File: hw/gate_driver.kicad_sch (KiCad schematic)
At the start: 0 parts

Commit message: parts of gate driver
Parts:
- added C501, C502: 10uF, Capacitor_SMD:C_0402_1005Metric, symbol Device:C_Small
- added R501, R502: 20k, Resistor_SMD:R_0402_1005Metric, symbol Device:R_Small
- added U501: LMG1210RVRT, IC_LMG1210RVRT, symbol LMG1210RVRT:LMG1210RVRT
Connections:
- new net: R502.1, U501.5 (DHL)
- new net: U501.13 (HS), U501.16 (HS), U501.21 (HS), U501.21_1 (HS), U501.21_2 (HS), U501.9 (HS)
- new net: R501.1, U501.6 (DLH)
- new net +12V: C502.1, U501.2 (VIN)
- new net +5V: C501.1, U501.4 (VDD)
- new net GND: C501.2, C502.2, R501.2, R502.2, U501.20 (VSS), U501.20_1 (VSS), U501.20_2 (VSS), U501.3 (VSS), U501.7 (VSS)
- new net PWM: U501.19 (PWM/LI)
- new net PWM_EN: U501.18 (EN/HI)
- new net SW1_OUT: U501.8 (LO)
- new net SW2_OUT: U501.10 (HO)
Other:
- note added: "Reselect after redeterming deadtime."

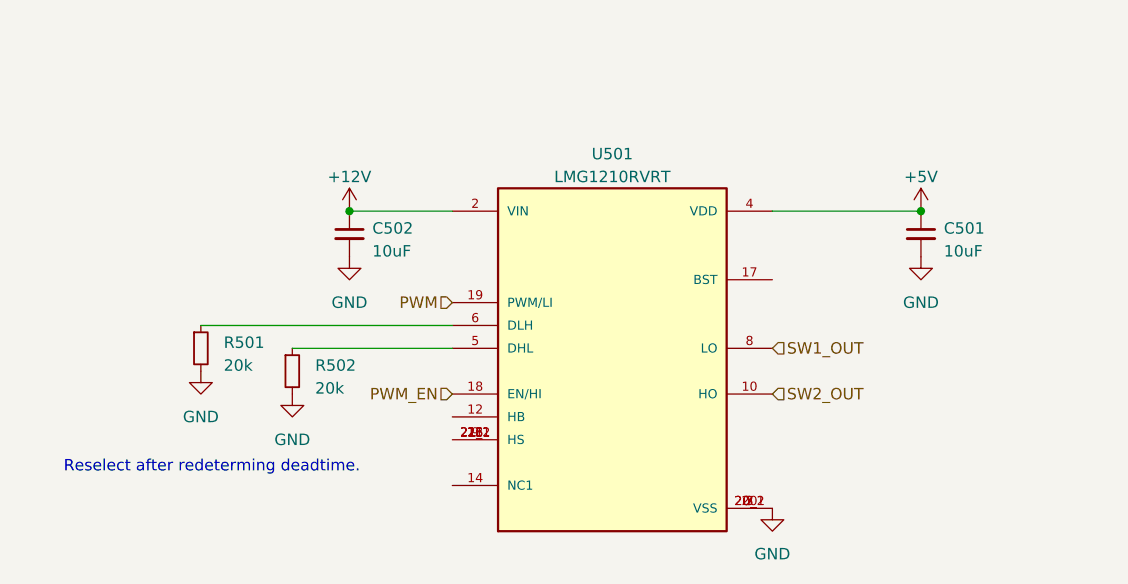
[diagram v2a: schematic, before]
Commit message: laid out MOSFET switching loop and thermal connections
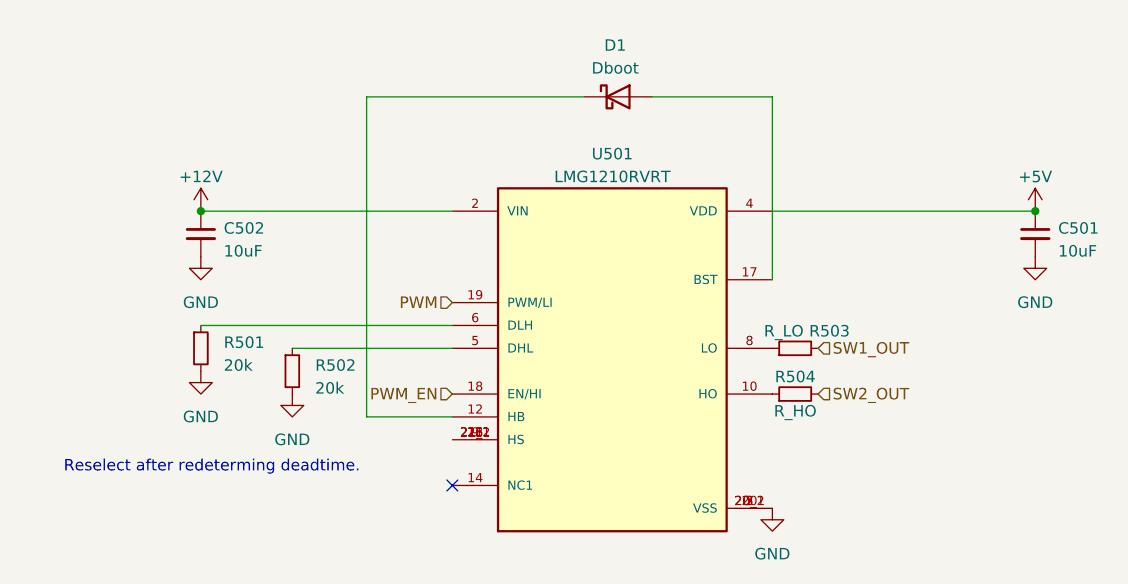
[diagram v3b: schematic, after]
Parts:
- added D1: Dboot, symbol Device:D_Schottky
- added R503: R_LO, Resistor_SMD:R_0402_1005Metric, symbol Device:R_Small
- added R504: R_HO, Resistor_SMD:R_0402_1005Metric, symbol Device:R_Small
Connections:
- net SW1_OUT: now also R503.2; no longer U501.8 (LO)
- net SW2_OUT: now also R504.2; no longer U501.10 (HO)
- net at U501.12 (HB): now also D1.1 (K)
- net at U501.17 (BST): now also D1.2 (A)
- new net: R504.1, U501.10 (HO)
- new net: R503.1, U501.8 (LO)
- no-connect marks 0 -> 1
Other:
- moved on the sheet: C501, C502

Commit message: made gate driver loop v1
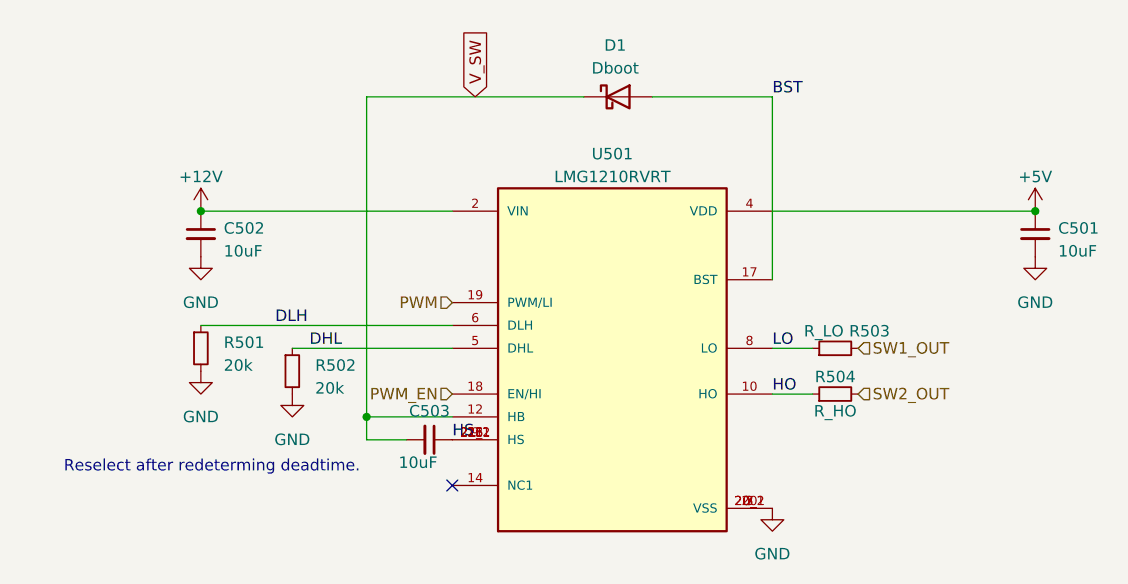
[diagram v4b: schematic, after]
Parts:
- added C503: 10uF, Capacitor_SMD:C_0402_1005Metric, symbol Device:C_Small
- C501: Mfg PN (none) -> GRM158R61A226ME15D
- C502: footprint Capacitor_SMD:C_0402_1005Metric -> Capacitor_SMD:C_0603_1608Metric; Mfg PN (none) -> CL10A226MO7JZNC
- D1: footprint (none) -> Diode_SMD:D_SOD-323
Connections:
- net HO: now reaches R504.1, U501.10 (HO)
- net LO: now reaches R503.1, U501.8 (LO)
- net V_SW: now reaches D1.1 (K), U501.12 (HB)
- net V_SW: now also C503.2
- net BST: now reaches D1.2 (A), U501.17 (BST)
- net DHL: now reaches R502.1, U501.5 (DHL)
- net HS: now reaches U501.13 (HS), U501.16 (HS), U501.21 (HS), U501.21_1 (HS), U501.21_2 (HS), U501.9 (HS)
- net HS: now also C503.1
- net DLH: now reaches R501.1, U501.6 (DLH)
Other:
- moved on the sheet: R503, R504
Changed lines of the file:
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@@
     (comment 2 "Jacob Pustilnik")
   )
+  (junction (at 128.905 101.6) (diameter 0) (color 0 0 0 0)
+  )
   (junction (at 203.2 78.74) (diameter 0) (color 0 0 0 0)
   )
@@
   )
   (no_connect (at 138.43 109.22))
-  (wire (pts (xy 128.905 101.6) (xy 128.905 66.04))
+  (wire (pts (xy 173.99 99.06) (xy 178.435 99.06))
+    (stroke (width 0) (type default))
+  )
+  (wire (pts (xy 128.905 66.04) (xy 128.905 101.6))
+    (stroke (width 0) (type default))
+  )
+  (wire (pts (xy 128.905 101.6) (xy 138.43 101.6))
     (stroke (width 0) (type default))
   )
@@
     (stroke (width 0) (type default))
   )
-  (wire (pts (xy 138.43 101.6) (xy 128.905 101.6))
-    (stroke (width 0) (type default))
-  )
   (wire (pts (xy 160.655 66.04) (xy 173.99 66.04))
     (stroke (width 0) (type default))
   )
+  (wire (pts (xy 173.99 93.98) (xy 178.435 93.98))
+    (stroke (width 0) (type default))
+  )
+  (wire (pts (xy 133.35 104.14) (xy 128.905 104.14))
+    (stroke (width 0) (type default))
+  )
   (wire (pts (xy 173.99 66.04) (xy 173.99 86.36))
     (stroke (width 0) (type default))
@@
     (stroke (width 0) (type default))
   )
+  (wire (pts (xy 128.905 101.6) (xy 128.905 104.14))
+    (stroke (width 0) (type default))
+  )
   (wire (pts (xy 110.49 91.44) (xy 138.43 91.44))
     (stroke (width 0) (type default))
@@
     (effects (font (size 1.27 1.27)) (justify left bottom))
   )
-  (hierarchical_label "SW2_OUT" (shape input) (at 179.07 99.06 0) (fields_autoplaced)
+  (label "DHL" (at 122.555 93.98 0) (fields_autoplaced)
+    (effects (font (size 1.27 1.27)) (justify left bottom))
+  )
+  (label "HO" (at 173.99 99.06 0) (fields_autoplaced)
+    (effects (font (size 1.27 1.27)) (justify left bottom))
+  )
+  (label "HS" (at 138.43 104.14 0) (fields_autoplaced)
+    (effects (font (size 1.27 1.27)) (justify left bottom))
+  )
+  (label "BST" (at 173.99 66.04 0) (fields_autoplaced)
+    (effects (font (size 1.27 1.27)) (justify left bottom))
+  )
+  (label "DLH" (at 118.745 91.44 0) (fields_autoplaced)
+    (effects (font (size 1.27 1.27)) (justify left bottom))
+  )
+  (label "LO" (at 173.99 93.98 0) (fields_autoplaced)
+    (effects (font (size 1.27 1.27)) (justify left bottom))
+  )
+  (global_label "V_SW" (shape input) (at 140.97 66.04 90) (fields_autoplaced)
+    (effects (font (size 1.27 1.27)) (justify left))
+    (property "Intersheetrefs" "${INTERSHEET_REFS}" (at 140.97 58.4171 90)
+      (effects (font (size 1.27 1.27)) (justify left) hide)
+    )
+  )
+  (hierarchical_label "SW2_OUT" (shape input) (at 183.515 99.06 0) (fields_autoplaced)
     (effects (font (size 1.27 1.27)) (justify left))
   )
@@
     (effects (font (size 1.27 1.27)) (justify right))
   )
-  (hierarchical_label "SW1_OUT" (shape input) (at 179.07 93.98 0) (fields_autoplaced)
+  (hierarchical_label "SW1_OUT" (shape input) (at 183.515 93.98 0) (fields_autoplaced)
     (effects (font (size 1.27 1.27)) (justify left))
   )
-  (symbol (lib_id "Device:R_Small") (at 176.53 99.06 90) (unit 1)
+  (symbol (lib_id "Device:R_Small") (at 180.975 99.06 90) (unit 1)
     (in_bom yes) (on_board yes) (dnp no)
-    (property "Reference" "R504" (at 176.53 97.155 90)
-      (effects (font (size 1.27 1.27)))
-    )
-    (property "Value" "R_HO" (at 176.53 100.965 90)
-      (effects (font (size 1.27 1.27)))
-    )
-    (property "Footprint" "Resistor_SMD:R_0402_1005Metric" (at 176.53 99.06 0)
-      (effects (font (size 1.27 1.27)) hide)
-    )
-    (property "Datasheet" "~" (at 176.53 99.06 0)
+    (property "Reference" "R504" (at 180.975 97.155 90)
+      (effects (font (size 1.27 1.27)))
+    )
+    (property "Value" "R_HO" (at 180.975 100.965 90)
+      (effects (font (size 1.27 1.27)))
+    )
+    (property "Footprint" "Resistor_SMD:R_0402_1005Metric" (at 180.975 99.06 0)
+      (effects (font (size 1.27 1.27)) hide)
+    )
+    (property "Datasheet" "~" (at 180.975 99.06 0)
       (effects (font (size 1.27 1.27)) hide)
     )
@@
       (effects (font (size 1.27 1.27)) hide)
     )
+    (property "Mfg PN" "GRM158R61A226ME15D" (at 203.2 81.28 0)
+      (effects (font (size 1.27 1.27)) hide)
+    )
     (pin "1")
     (pin "2")
@@
     )
   )
-  (symbol (lib_id "Device:R_Small") (at 176.53 93.98 90) (unit 1)
+  (symbol (lib_id "Device:R_Small") (at 180.975 93.98 90) (unit 1)
     (in_bom yes) (on_board yes) (dnp no)
-    (property "Reference" "R503" (at 180.34 92.075 90)
-      (effects (font (size 1.27 1.27)))
-    )
-    (property "Value" "R_LO" (at 175.26 92.075 90)
-      (effects (font (size 1.27 1.27)))
-    )
-    (property "Footprint" "Resistor_SMD:R_0402_1005Metric" (at 176.53 93.98 0)
-      (effects (font (size 1.27 1.27)) hide)
-    )
-    (property "Datasheet" "~" (at 176.53 93.98 0)
+    (property "Reference" "R503" (at 184.785 92.075 90)
+      (effects (font (size 1.27 1.27)))
+    )
+    (property "Value" "R_LO" (at 179.705 92.075 90)
+      (effects (font (size 1.27 1.27)))
+    )
+    (property "Footprint" "Resistor_SMD:R_0402_1005Metric" (at 180.975 93.98 0)
+      (effects (font (size 1.27 1.27)) hide)
+    )
+    (property "Datasheet" "~" (at 180.975 93.98 0)
       (effects (font (size 1.27 1.27)) hide)
     )
@@
       (effects (font (size 1.27 1.27)))
     )
-    (property "Footprint" "" (at 156.845 66.04 0)
+    (property "Footprint" "Diode_SMD:D_SOD-323" (at 156.845 66.04 0)
       (effects (font (size 1.27 1.27)) hide)
     )
@@
         (path "/06fd3a42-664d-41bc-bf0f-b5ee0ddcc902/d2872b58-d342-47d2-86ca-67a04f8e2122"
           (reference "#PWR0501") (unit 1)
+        )
+      )
+    )
+  )
+  (symbol (lib_id "Device:C_Small") (at 135.89 104.14 270) (unit 1)
+    (in_bom yes) (on_board yes) (dnp no)
+    (property "Reference" "C503" (at 135.89 100.965 90)
+      (effects (font (size 1.27 1.27)))
+    )
+    (property "Value" "10uF" (at 134.62 106.68 90)
+      (effects (font (size 1.27 1.27)))
+    )
+    (property "Footprint" "Capacitor_SMD:C_0402_1005Metric" (at 135.89 104.14 0)
+      (effects (font (size 1.27 1.27)) hide)
+    )
+    (property "Datasheet" "~" (at 135.89 104.14 0)
+      (effects (font (size 1.27 1.27)) hide)
+    )
+    (property "Mfr PN" "GRM158R61A226ME15D" (at 135.89 104.14 90)
+      (effects (font (size 1.27 1.27)) hide)
+    )
+    (pin "1")
+    (pin "2")
+    (instances
+      (project "mppt"
+        (path "/06fd3a42-664d-41bc-bf0f-b5ee0ddcc902/d2872b58-d342-47d2-86ca-67a04f8e2122"
+          (reference "C503") (unit 1)
         )
       )
@@
       (effects (font (size 1.27 1.27)) (justify left))
     )
-    (property "Footprint" "Capacitor_SMD:C_0402_1005Metric" (at 110.49 81.28 0)
+    (property "Footprint" "Capacitor_SMD:C_0603_1608Metric" (at 110.49 81.28 0)
       (effects (font (size 1.27 1.27)) hide)
     )
@@
       (effects (font (size 1.27 1.27)) hide)
     )
+    (property "Mfg PN" "CL10A226MO7JZNC" (at 110.49 81.28 0)
+      (effects (font (size 1.27 1.27)) hide)
+    )

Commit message: layout revision this one is cursed
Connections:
- net BST is gone; now on net +5V: D1.2 (A), U501.17 (BST)
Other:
- moved on the sheet: C501, D1, R503, R504

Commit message: slight bom updates
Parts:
- C501: In Stock? (none) -> Y; Mfg PN GRM158R61A226ME15D -> (none); Mfr PN (none) -> GRM158R61A226ME15D; Projected Cost (none) -> 0.48
- C502: In Stock? (none) -> Y; Projected Cost (none) -> 0.61
- C503: In Stock? (none) -> Y; Projected Cost (none) -> 0.48
- D1: In Stock? (none) -> Y; Projected Cost (none) -> 0.51
- U501: In Stock? (none) -> Y; Projected Cost (none) -> 4.10
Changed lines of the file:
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@@
       (effects (font (size 1.27 1.27)) hide)
     )
-    (property "Mfg PN" "GRM158R61A226ME15D" (at 181.61 81.28 0)
+    (property "Mfr PN" "GRM158R61A226ME15D" (at 181.61 81.28 0)
+      (effects (font (size 1.27 1.27)) hide)
+    )
+    (property "Projected Cost" "0.48" (at 181.61 81.28 0)
+      (effects (font (size 1.27 1.27)) hide)
+    )
+    (property "In Stock?" "Y" (at 181.61 81.28 0)
       (effects (font (size 1.27 1.27)) hide)
     )
@@
       (effects (font (size 1.27 1.27)) hide)
     )
+    (property "Projected Cost" "0.51" (at 156.21 66.04 0)
+      (effects (font (size 1.27 1.27)) hide)
+    )
+    (property "In Stock?" "Y" (at 156.21 66.04 0)
+      (effects (font (size 1.27 1.27)) hide)
+    )
     (pin "1")
     (pin "2")
@@
       (effects (font (size 1.27 1.27)) hide)
     )
+    (property "Projected Cost" "0.48" (at 135.89 104.14 90)
+      (effects (font (size 1.27 1.27)) hide)
+    )
+    (property "In Stock?" "Y" (at 135.89 104.14 90)
+      (effects (font (size 1.27 1.27)) hide)
+    )
     (pin "1")
     (pin "2")
@@
       (effects (font (size 1.27 1.27)) hide)
     )
+    (property "Projected Cost" "0.61" (at 110.49 81.28 0)
+      (effects (font (size 1.27 1.27)) hide)
+    )
+    (property "In Stock?" "Y" (at 110.49 81.28 0)
+      (effects (font (size 1.27 1.27)) hide)
+    )
     (pin "1")
     (pin "2")
@@
       (effects (font (size 1.27 1.27)) (justify bottom) hide)
     )
+    (property "Projected Cost" "4.10" (at 156.21 96.52 0)
+      (effects (font (size 1.27 1.27)) hide)
+    )
+    (property "In Stock?" "Y" (at 156.21 96.52 0)
+      (effects (font (size 1.27 1.27)) hide)
+    )
     (pin "10")

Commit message: revision of PCB layout
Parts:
- C502: footprint Capacitor_SMD:C_0603_1608Metric -> Capacitor_SMD:C_0402_1005Metric
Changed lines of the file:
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@@
       (effects (font (size 1.27 1.27)) (justify left))
     )
-    (property "Footprint" "Capacitor_SMD:C_0603_1608Metric" (at 110.49 81.28 0)
+    (property "Footprint" "Capacitor_SMD:C_0402_1005Metric" (at 110.49 81.28 0)
       (effects (font (size 1.27 1.27)) hide)
     )
@@
   )
   (symbol (lib_id "Device:R_Small") (at 120.65 96.52 0) (unit 1)
-    (in_bom yes) (on_board yes) (dnp no) (fields_autoplaced)
+    (in_bom yes) (on_board yes) (dnp no)
     (property "Reference" "R502" (at 123.19 95.885 0)
       (effects (font (size 1.27 1.27)) (justify left))

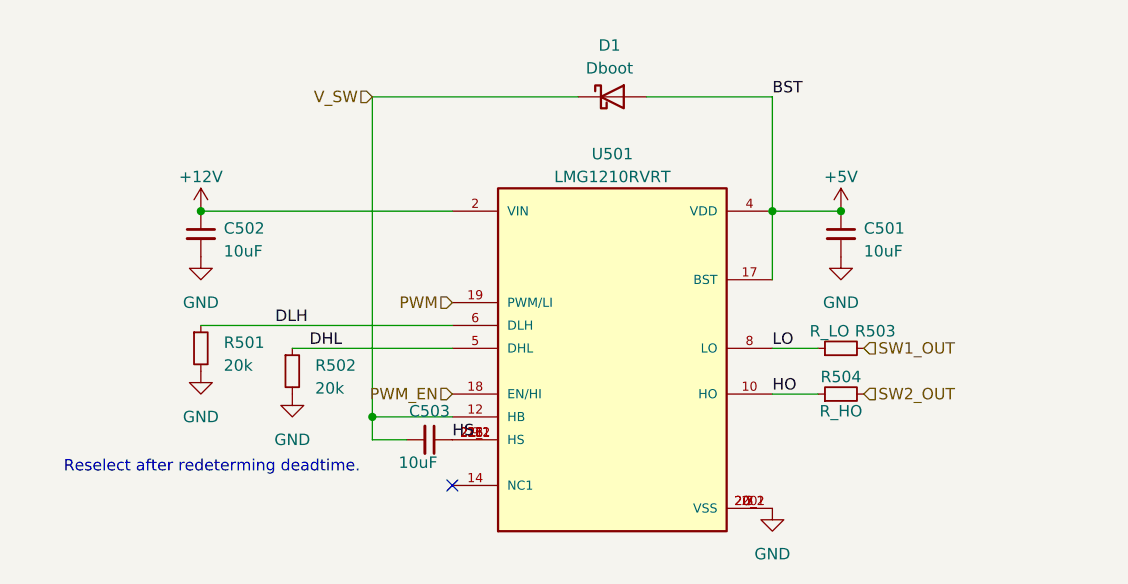
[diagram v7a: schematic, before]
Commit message: segregating code into design procedures
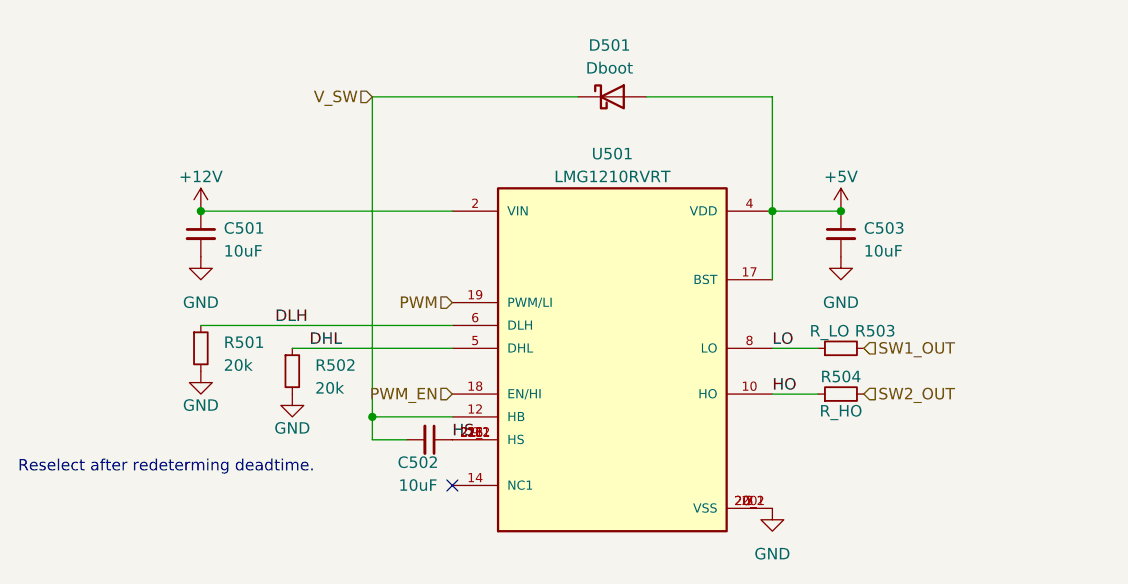
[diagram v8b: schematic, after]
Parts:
- renumbered C502 to C501, C503 to C502, C501 to C503, D1 to D501
